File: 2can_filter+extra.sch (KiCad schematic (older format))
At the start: 17 parts

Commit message: finish scheme & change libs path
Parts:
- removed C? (x2): 12pF, symbol C
- removed D?: PMLL4148L.115, Diodes_SMD:D_SC-80, symbol D
- removed J?: NOT_FITTED_SWD_Conn_01x04_Male, symbol Conn_01x04_Male
- removed J?: USB_OTG, symbol USB_OTG
- removed R? (x2): 60, symbol R
- removed R?: 10k, symbol R
- removed U?: TJA1040T, Housings_SOIC:SOIC-8_3.9x4.9mm_Pitch1.27mm, symbol TJA1040T
- removed Y?: Crystal KX-7 25MHz, symbol Crystal
- added C13, C14: 12pF, symbol C
- added C15: 1nF, symbol C
- added D8, D9: PMLL4148L.115, Diodes_SMD:D_SC-80, symbol D
- added J5: 54819-0572, 54819-0572:MOLEXMINIBTYPEB_1, symbol 54819-0572
- added J6: NOT_FITTED_SWD_Conn_01x04_Male, symbol Conn_01x04_Male
- added R10, R9: 2.2k, symbol R
- added R11: 1k5, symbol R
- added R12, R15: 1k, symbol R
- added R13: 10k, symbol R
- added R18, R19: 60, symbol R
- added R7, R8: 9k, symbol R
- added R? (x2): 22, symbol R
- added U10, U8: 74HC4050D, Housings_SOIC:SOIC-16_3.9x9.9mm_Pitch1.27mm, symbol 74HC4050D
- added U11: TJA1021T, Housings_SOIC:SOIC-8_3.9x4.9mm_Pitch1.27mm, symbol TJA1021T
- added U13: TJA1040T, Housings_SOIC:SOIC-8_3.9x4.9mm_Pitch1.27mm, symbol TJA1040T
- added Y2: Crystal KX-7 25MHz, symbol Crystal
- U9: renamed from U?; footprint LQFP64 -> Housings_QFP:LQFP-64_10x10mm_Pitch0.5mm
- gave numbers to parts that had none: 6
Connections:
- net labels added: ANTI-THEFT, BELT_MINDER, BRAKE(fluid_level), ENGINE(coolant_level), FUEL_ADC_1, FUEL_ADC_2, ILLUM, LAW_WASHER(fluid_level), LIN, LIN_+12V, LIN_RXD, LIN_SLP, LIN_TXD, OIL(pressure_level), PAD-WEAR, PARKING-BRAKE, TRIP_COMPUTER, anti-theft, belt, brake_fluid_level, engine_coolant, fuel_adc_1, fuel_adc_2, illum, oil_pressure_level, pad_wear, parking_brakes, trip_comp, washer
- wire segments 63 -> 93
- no-connect marks 3 -> 35
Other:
- moved on the sheet: C16, C17, R14, R16, R17, U12, U9

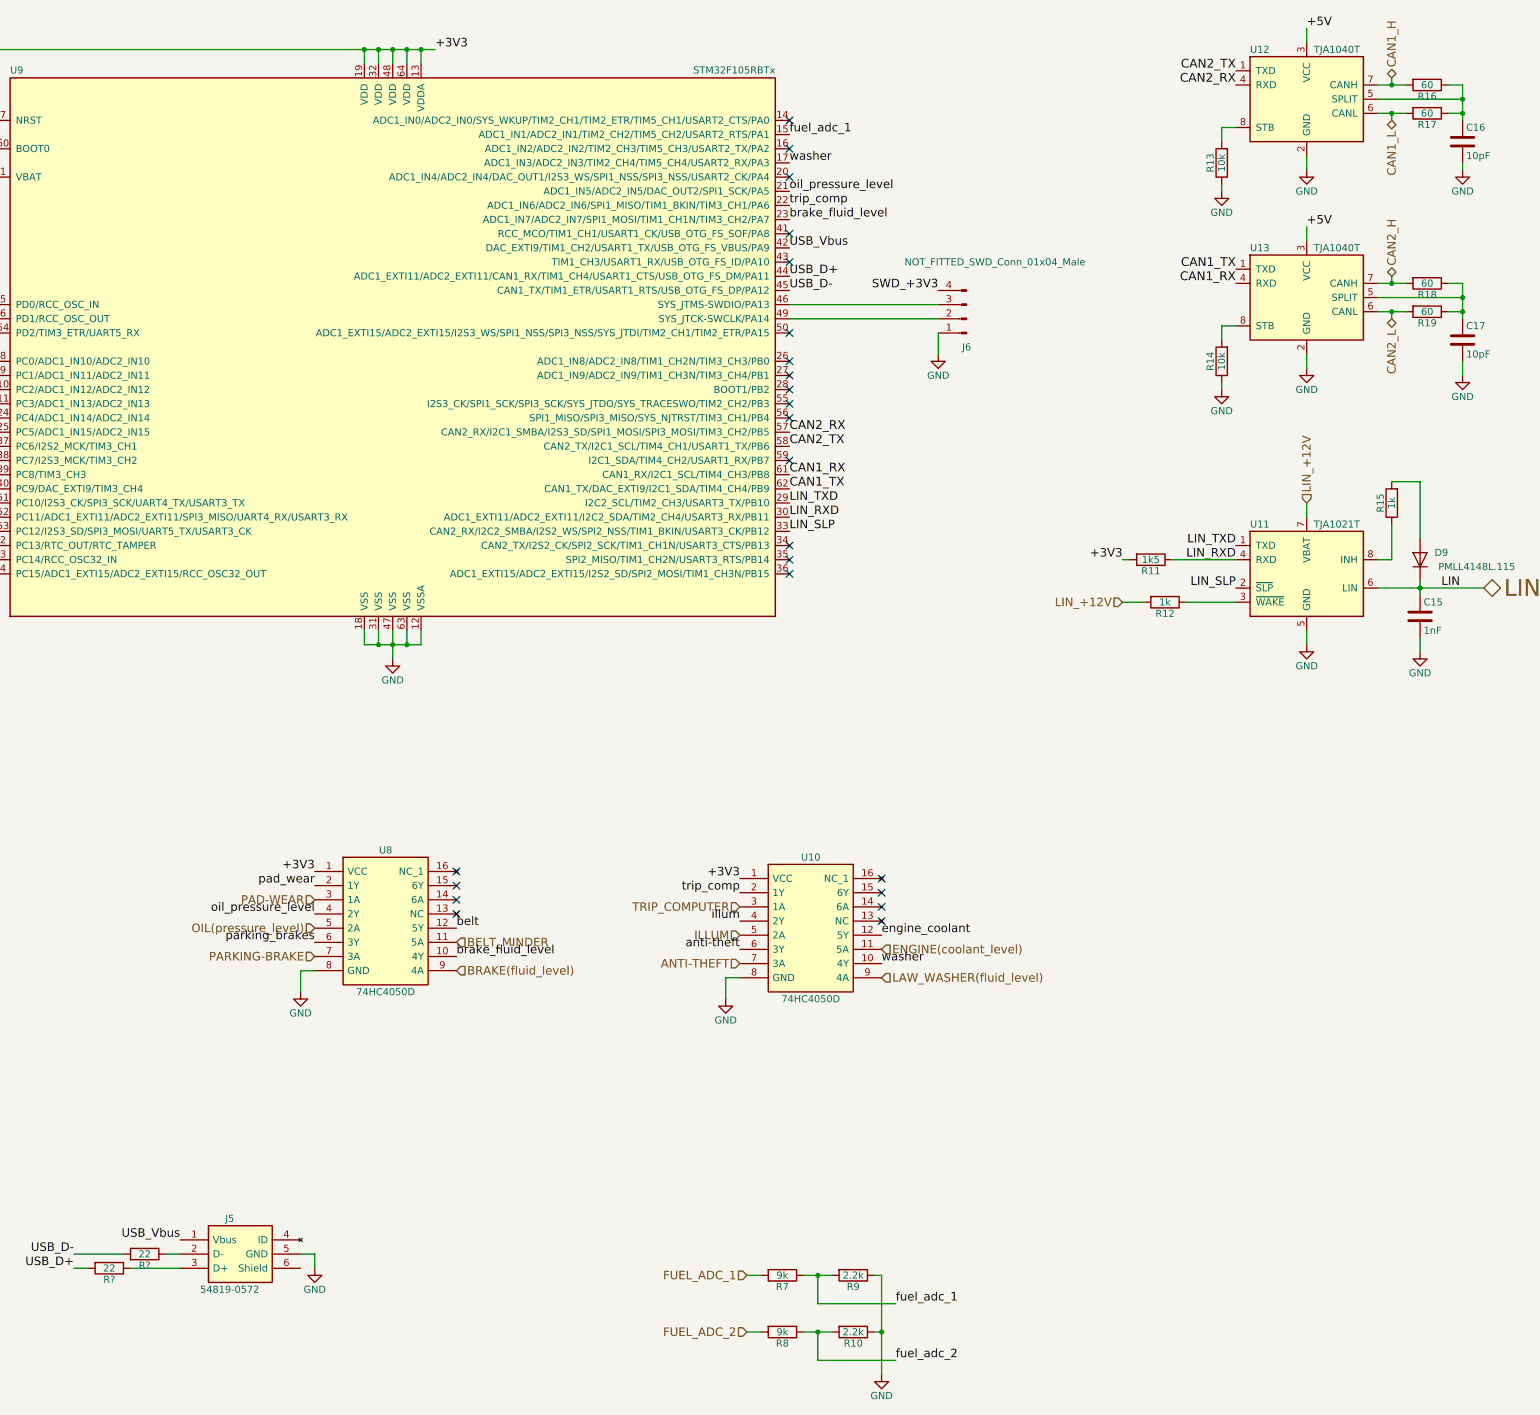
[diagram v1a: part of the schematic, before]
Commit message: specify footpints to resistors and capasitors
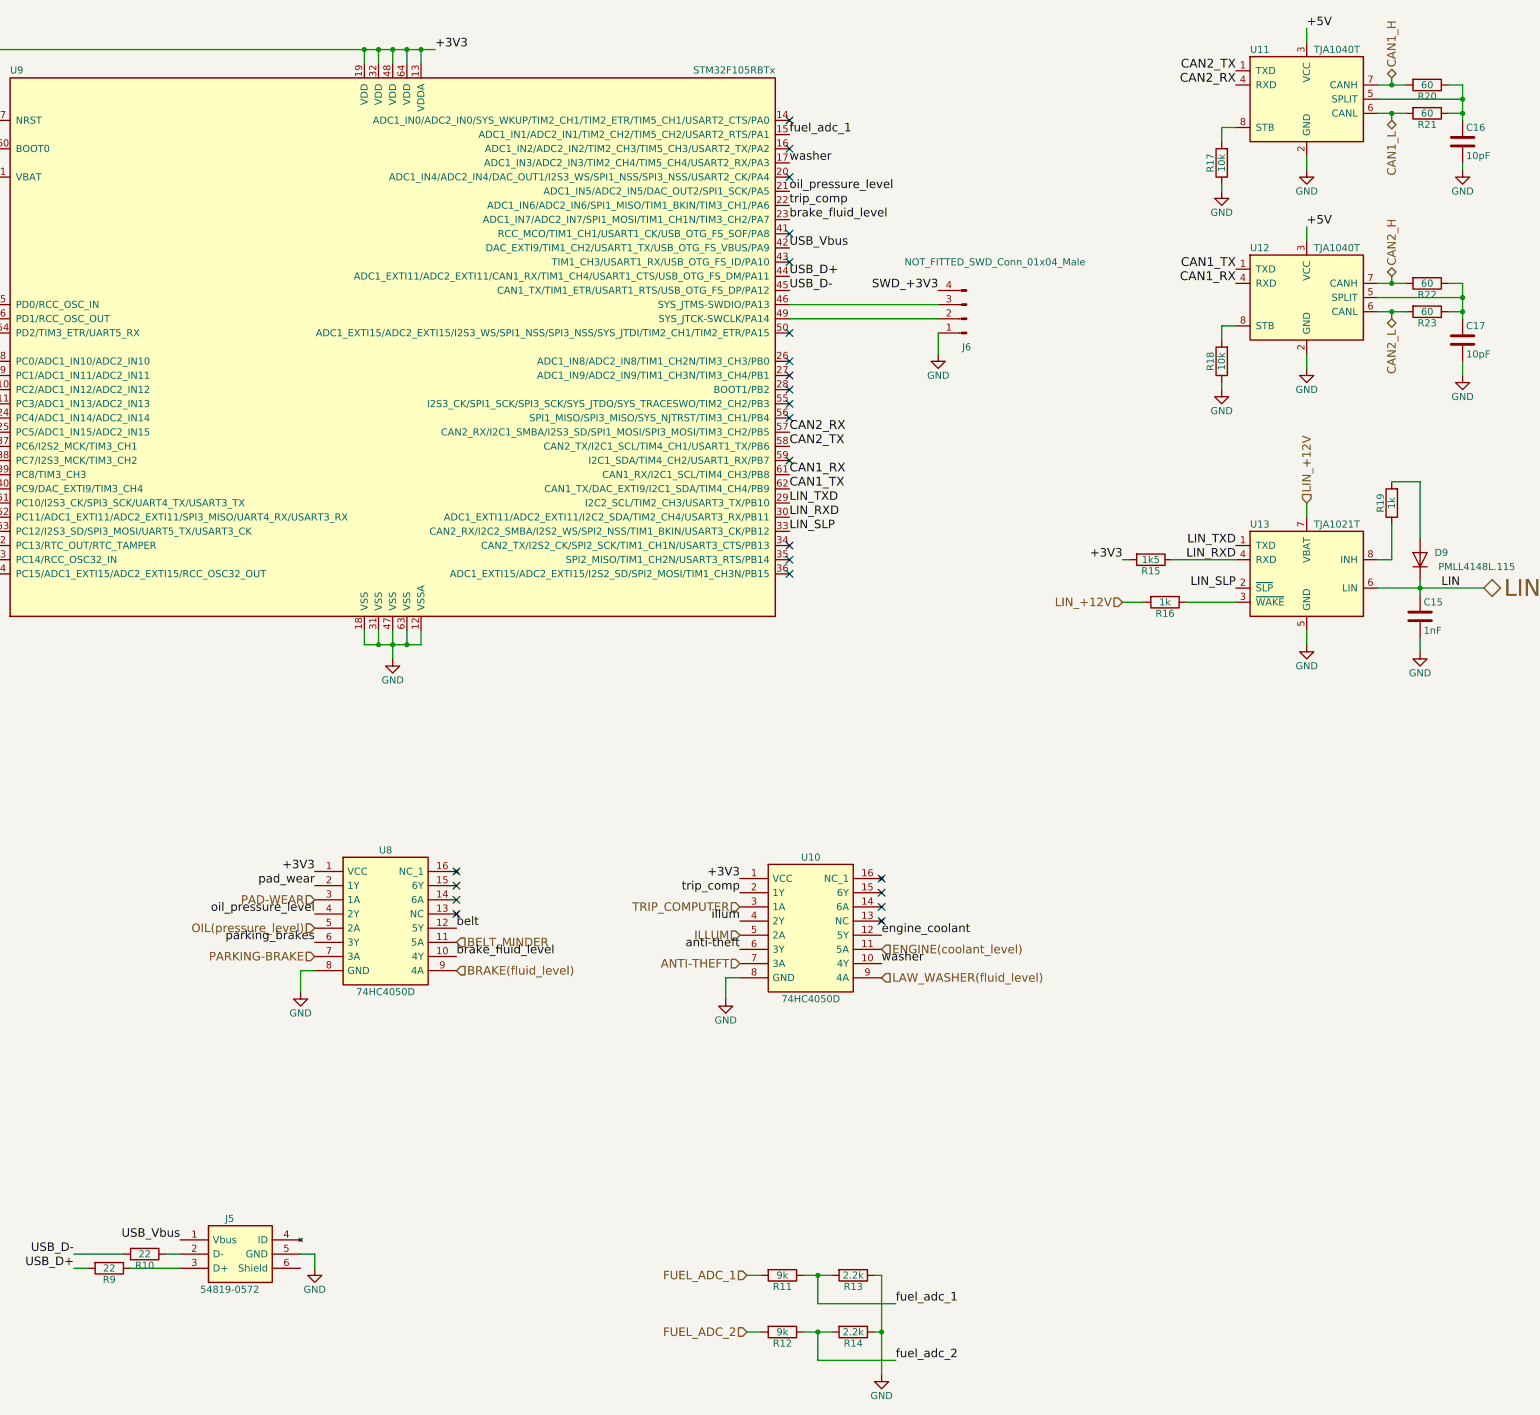
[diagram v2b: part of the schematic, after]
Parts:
- C13, C14, C15, C16, C17: footprint (none) -> Capacitors_SMD:C_0805
- R10, R9: renamed from R?; footprint (none) -> Resistors_SMD:R_0805
- R11: renamed from R7; footprint (none) -> Resistors_SMD:R_0805
- R12: renamed from R8; footprint (none) -> Resistors_SMD:R_0805
- R13: renamed from R9; footprint (none) -> Resistors_SMD:R_0805
- R14: renamed from R10; footprint (none) -> Resistors_SMD:R_0805
- R15: renamed from R11; footprint (none) -> Resistors_SMD:R_0805
- R16: renamed from R12; footprint (none) -> Resistors_SMD:R_0805
- R17: renamed from R13; footprint (none) -> Resistors_SMD:R_0805
- R18: renamed from R14; footprint (none) -> Resistors_SMD:R_0805
- R19: renamed from R15; footprint (none) -> Resistors_SMD:R_0805
- R20: renamed from R16; footprint (none) -> Resistors_SMD:R_0805
- R21: renamed from R17; footprint (none) -> Resistors_SMD:R_0805
- R22: renamed from R18; footprint (none) -> Resistors_SMD:R_0805
- R23: renamed from R19; footprint (none) -> Resistors_SMD:R_0805
- renumbered U12 to U11, U13 to U12, U11 to U13

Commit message: add missed footprints, add additional capasitors on 3.3V line, fix banch of ERC errors
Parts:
- removed Y2: Crystal KX-7 25MHz, symbol Crystal
- added Y2: Crystal KX-13 25MHz, Crystals:Crystal_SMD_7050-4pin_7.0x5.0mm, symbol Crystal_GND24
- C25: renamed from C13; value 12pF -> 16pF
- C26: renamed from C14; value 12pF -> 16pF
- renumbered C15 to C27, C16 to C28, C17 to C29
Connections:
- wire segments 93 -> 98
- no-connect marks 35 -> 31
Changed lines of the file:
@@
 	1800 9950 2250 9950
 $Comp
-L C C16
+L C C28
 U 1 1 5A047AB3
 P 14500 1900
-F 0 "C16" H 14525 2000 50  0000 L CNN
+F 0 "C28" H 14525 2000 50  0000 L CNN
 F 1 "10pF" H 14525 1800 50  0000 L CNN
 F 2 "Capacitors_SMD:C_0805" H 14538 1750 50  0001 C CNN
@@
 +3V3
 $Comp
-L GND #PWR24
+L GND #PWR030
 U 1 1 5A047DA1
 P 2050 10050
-F 0 "#PWR24" H 2050 9800 50  0001 C CNN
+F 0 "#PWR030" H 2050 9800 50  0001 C CNN
 F 1 "GND" H 2050 9900 50  0000 C CNN
 F 2 "" H 2050 10050 50  0001 C CNN
@@
 Connection ~ 6850 5450
 $Comp
-L GND #PWR29
+L GND #PWR031
 U 1 1 5A0480FC
 P 6950 5550
-F 0 "#PWR29" H 6950 5300 50  0001 C CNN
+F 0 "#PWR031" H 6950 5300 50  0001 C CNN
 F 1 "GND" H 6950 5400 50  0000 C CNN
 F 2 "" H 6950 5550 50  0001 C CNN
@@
 Connection ~ 14500 1600
 $Comp
-L C C17
+L C C29
 U 1 1 5A048753
 P 14500 3300
-F 0 "C17" H 14525 3400 50  0000 L CNN
+F 0 "C29" H 14525 3400 50  0000 L CNN
 F 1 "10pF" H 14525 3200 50  0000 L CNN
 F 2 "Capacitors_SMD:C_0805" H 14538 3150 50  0001 C CNN
@@
 	12800 2200 12800 2250
 $Comp
-L GND #PWR35
+L GND #PWR032
 U 1 1 5A09EB23
 P 13400 2100
-F 0 "#PWR35" H 13400 1850 50  0001 C CNN
+F 0 "#PWR032" H 13400 1850 50  0001 C CNN
 F 1 "GND" H 13400 1950 50  0000 C CNN
 F 2 "" H 13400 2100 50  0001 C CNN
@@
 	13400 2000 13400 2100
 $Comp
-L GND #PWR39
+L GND #PWR033
 U 1 1 5A048D93
 P 14500 2100
-F 0 "#PWR39" H 14500 1850 50  0001 C CNN
+F 0 "#PWR033" H 14500 1850 50  0001 C CNN
 F 1 "GND" H 14500 1950 50  0000 C CNN
 F 2 "" H 14500 2100 50  0001 C CNN
@@
 	14500 2100 14500 2050
 $Comp
-L GND #PWR33
+L GND #PWR034
 U 1 1 5A048E0B
 P 12800 2250
-F 0 "#PWR33" H 12800 2000 50  0001 C CNN
+F 0 "#PWR034" H 12800 2000 50  0001 C CNN
 F 1 "GND" H 12800 2100 50  0000 C CNN
 F 2 "" H 12800 2250 50  0001 C CNN
@@
 	12800 3600 12800 3650
 $Comp
-L GND #PWR34
+L GND #PWR035
 U 1 1 5A048FA0
 P 12800 3650
-F 0 "#PWR34" H 12800 3400 50  0001 C CNN
+F 0 "#PWR035" H 12800 3400 50  0001 C CNN
 F 1 "GND" H 12800 3500 50  0000 C CNN
 F 2 "" H 12800 3650 50  0001 C CNN
@@
 $EndComp
 $Comp
-L GND #PWR36
+L GND #PWR036
 U 1 1 5A049172
 P 13400 3500
-F 0 "#PWR36" H 13400 3250 50  0001 C CNN
+F 0 "#PWR036" H 13400 3250 50  0001 C CNN
 F 1 "GND" H 13400 3350 50  0000 C CNN
 F 2 "" H 13400 3500 50  0001 C CNN
@@
 	13400 3400 13400 3500
 $Comp
-L GND #PWR40
+L GND #PWR037
 U 1 1 5A09EB29
 P 14500 3550
-F 0 "#PWR40" H 14500 3300 50  0001 C CNN
+F 0 "#PWR037" H 14500 3300 50  0001 C CNN
 F 1 "GND" H 14500 3400 50  0000 C CNN
 F 2 "" H 14500 3550 50  0001 C CNN
@@
 	10800 3400 10800 3250
 $Comp
-L GND #PWR32
+L GND #PWR038
 U 1 1 5A09EB2C
 P 10800 3400
-F 0 "#PWR32" H 10800 3150 50  0001 C CNN
+F 0 "#PWR038" H 10800 3150 50  0001 C CNN
 F 1 "GND" H 10800 3250 50  0000 C CNN
 F 2 "" H 10800 3400 50  0001 C CNN
@@
 Connection ~ 2900 9950
 $Comp
-L Crystal Y2
-U 1 1 5A09EB2D
-P 2450 3600
-F 0 "Y2" H 2450 3750 50  0000 C CNN
-F 1 "Crystal KX-7 25MHz" H 2400 3900 50  0000 C CNN
-F 2 "" H 2450 3600 50  0001 C CNN
-F 3 "" H 2450 3600 50  0001 C CNN
-	1    2450 3600
-	1    0    0    -1
-$EndComp
-$Comp
-L C C14
+L C C26
 U 1 1 5A09EB2E
 P 2750 3850
-F 0 "C14" H 2775 3950 50  0000 L CNN
-F 1 "12pF" H 2775 3750 50  0000 L CNN
+F 0 "C26" H 2775 3950 50  0000 L CNN
+F 1 "16pF" H 2775 3750 50  0000 L CNN
 F 2 "Capacitors_SMD:C_0805" H 2788 3700 50  0001 C CNN
 F 3 "" H 2750 3850 50  0001 C CNN
@@
 $EndComp
 $Comp
-L C C13
+L C C25
 U 1 1 5A09EB2F
 P 2150 3850
-F 0 "C13" H 2175 3950 50  0000 L CNN
-F 1 "12pF" H 2175 3750 50  0000 L CNN
+F 0 "C25" H 2175 3950 50  0000 L CNN
+F 1 "16pF" H 2175 3750 50  0000 L CNN
 F 2 "Capacitors_SMD:C_0805" H 2188 3700 50  0001 C CNN
 F 3 "" H 2150 3850 50  0001 C CNN
@@
 $EndComp
 $Comp
-L GND #PWR25
-U 1 1 5A09EB30
-P 2150 4100
-F 0 "#PWR25" H 2150 3850 50  0001 C CNN
-F 1 "GND" H 2150 3950 50  0000 C CNN
-F 2 "" H 2150 4100 50  0001 C CNN
-F 3 "" H 2150 4100 50  0001 C CNN
-	1    2150 4100
-	1    0    0    -1
-$EndComp
-$Comp
-L GND #PWR26
+L GND #PWR039
 U 1 1 5A09EB31
-P 2750 4100
-F 0 "#PWR26" H 2750 3850 50  0001 C CNN
-F 1 "GND" H 2750 3950 50  0000 C CNN
-F 2 "" H 2750 4100 50  0001 C CNN
-F 3 "" H 2750 4100 50  0001 C CNN
-	1    2750 4100
-	1    0    0    -1
-$EndComp
-Wire Wire Line
-	2150 4000 2150 4100
-Wire Wire Line
-	2750 4000 2750 4100
+P 2450 4050
+F 0 "#PWR039" H 2450 3800 50  0001 C CNN
+F 1 "GND" H 2450 3900 50  0000 C CNN
+F 2 "" H 2450 4050 50  0001 C CNN
+F 3 "" H 2450 4050 50  0001 C CNN
+	1    2450 4050
+	1    0    0    -1
+$EndComp
+Wire Wire Line
+	2150 4000 2150 4050
+Wire Wire Line
+	2750 4050 2750 4000
 Wire Wire Line
 	2150 3050 2150 3700
@@
 Connection ~ 2750 3600
 $Comp
-L GND #PWR28
+L GND #PWR040
 U 1 1 5A09EB32
-P 6400 9850
-F 0 "#PWR28" H 6400 9600 50  0001 C CNN
-F 1 "GND" H 6400 9700 50  0000 C CNN
-F 2 "" H 6400 9850 50  0001 C CNN
-F 3 "" H 6400 9850 50  0001 C CNN
-	1    6400 9850
+P 6400 9900
+F 0 "#PWR040" H 6400 9650 50  0001 C CNN
+F 1 "GND" H 6400 9750 50  0000 C CNN
+F 2 "" H 6400 9900 50  0001 C CNN
+F 3 "" H 6400 9900 50  0001 C CNN
+	1    6400 9900
 	1    0    0    -1
 $EndComp
@@
 	6300 9750 6400 9750
 Wire Wire Line
-	6400 9750 6400 9850
+	6400 9750 6400 9900
 $Comp
 L TJA1021T U13
@@
 Text Label 6400 7050 2    60   ~ 0
 +3V3
-NoConn ~ 10400 7100
-NoConn ~ 10400 7400
-NoConn ~ 7400 7050
-NoConn ~ 7400 7350
 $Comp
 L R R11
@@
 Connection ~ 9950 10300
 $Comp
-L GND #PWR31
+L GND #PWR041
 U 1 1 5A09F076
 P 10400 10600
-F 0 "#PWR31" H 10400 10350 50  0001 C CNN
+F 0 "#PWR041" H 10400 10350 50  0001 C CNN
 F 1 "GND" H 10400 10450 50  0000 C CNN
 F 2 "" H 10400 10600 50  0001 C CNN
@@
 anti-theft
 $Comp
-L GND #PWR27
+L GND #PWR042
 U 1 1 5A0A1F34
-P 6300 7900
-F 0 "#PWR27" H 6300 7650 50  0001 C CNN
-F 1 "GND" H 6300 7750 50  0000 C CNN
-F 2 "" H 6300 7900 50  0001 C CNN
-F 3 "" H 6300 7900 50  0001 C CNN
-	1    6300 7900
-	1    0    0    -1
-$EndComp
-Wire Wire Line
-	6300 7750 6300 7900
+P 6300 7850
+F 0 "#PWR042" H 6300 7600 50  0001 C CNN
+F 1 "GND" H 6300 7700 50  0000 C CNN
+F 2 "" H 6300 7850 50  0001 C CNN
+F 3 "" H 6300 7850 50  0001 C CNN
+	1    6300 7850
+	1    0    0    -1
+$EndComp
+Wire Wire Line
+	6300 7750 6300 7850
 Wire Wire Line
 	6300 7750 6400 7750
-$Comp
-L GND #PWR30
-U 1 1 5A0A211A
-P 9300 7950
-F 0 "#PWR30" H 9300 7700 50  0001 C CNN
-F 1 "GND" H 9300 7800 50  0000 C CNN
-F 2 "" H 9300 7950 50  0001 C CNN
-F 3 "" H 9300 7950 50  0001 C CNN
-	1    9300 7950
-	1    0    0    -1
-$EndComp
-Wire Wire Line
-	9300 7800 9300 7950
-Wire Wire Line
-	9300 7800 9400 7800
 Text Label 10400 7700 0    60   ~ 0
 washer
@@
 $EndComp
 $Comp
-L C C15
+L C C27
 U 1 1 5A0B8E49
 P 14200 5250
-F 0 "C15" H 14225 5350 50  0000 L CNN
+F 0 "C27" H 14225 5350 50  0000 L CNN
 F 1 "1nF" H 14225 5150 50  0000 L CNN
 F 2 "Capacitors_SMD:C_0805" H 14238 5100 50  0001 C CNN
@@
 Connection ~ 14200 5050
 $Comp
-L GND #PWR37
+L GND #PWR043
 U 1 1 5A0BEC86
 P 13400 5450
-F 0 "#PWR37" H 13400 5200 50  0001 C CNN
+F 0 "#PWR043" H 13400 5200 50  0001 C CNN
 F 1 "GND" H 13400 5300 50  0000 C CNN
 F 2 "" H 13400 5450 50  0001 C CNN
@@
 $EndComp
 $Comp
-L GND #PWR38
+L GND #PWR044
 U 1 1 5A0BECD4
 P 14200 5500
-F 0 "#PWR38" H 14200 5250 50  0001 C CNN
+F 0 "#PWR044" H 14200 5250 50  0001 C CNN
 F 1 "GND" H 14200 5350 50  0000 C CNN
 F 2 "" H 14200 5500 50  0001 C CNN
@@
 Wire Wire Line
 	5350 9750 5450 9750
+$Comp
+L Crystal_GND24 Y2
+U 1 1 5A0DB947
+P 2450 3600
+F 0 "Y2" H 2575 3800 50  0000 L CNN
+F 1 "Crystal KX-13 25MHz" H 2575 3725 50  0000 L CNN
+F 2 "Crystals:Crystal_SMD_7050-4pin_7.0x5.0mm" H 2450 3600 50  0001 C CNN
+F 3 "" H 2450 3600 50  0001 C CNN
+	1    2450 3600
+	1    0    0    -1
+$EndComp
+Wire Wire Line
+	2450 4050 2450 3800
+Wire Wire Line
+	1900 4050 2750 4050
+Connection ~ 2450 4050
+Wire Wire Line
+	2450 3400 1900 3400
+Wire Wire Line
+	1900 3400 1900 4050
+Connection ~ 2150 4050
+Wire Wire Line
+	6300 9850 6400 9850
+Connection ~ 6400 9850
+$Comp
+L GND #PWR045
+U 1 1 5A0EC5D8
+P 9300 7950
+F 0 "#PWR045" H 9300 7700 50  0001 C CNN
+F 1 "GND" H 9300 7800 50  0000 C CNN
+F 2 "" H 9300 7950 50  0001 C CNN
+F 3 "" H 9300 7950 50  0001 C CNN
+	1    9300 7950
+	1    0    0    -1
+$EndComp
+Wire Wire Line
+	9300 7950 9300 7800
+Wire Wire Line
+	9300 7800 9400 7800
 $EndSCHEMATC
